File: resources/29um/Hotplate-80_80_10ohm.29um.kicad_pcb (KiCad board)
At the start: 2 copper layers, 80 x 80 mm, 7 parts, among them J1 Hotplate_Power_Connection, J2 Hotplate_Power_Connection

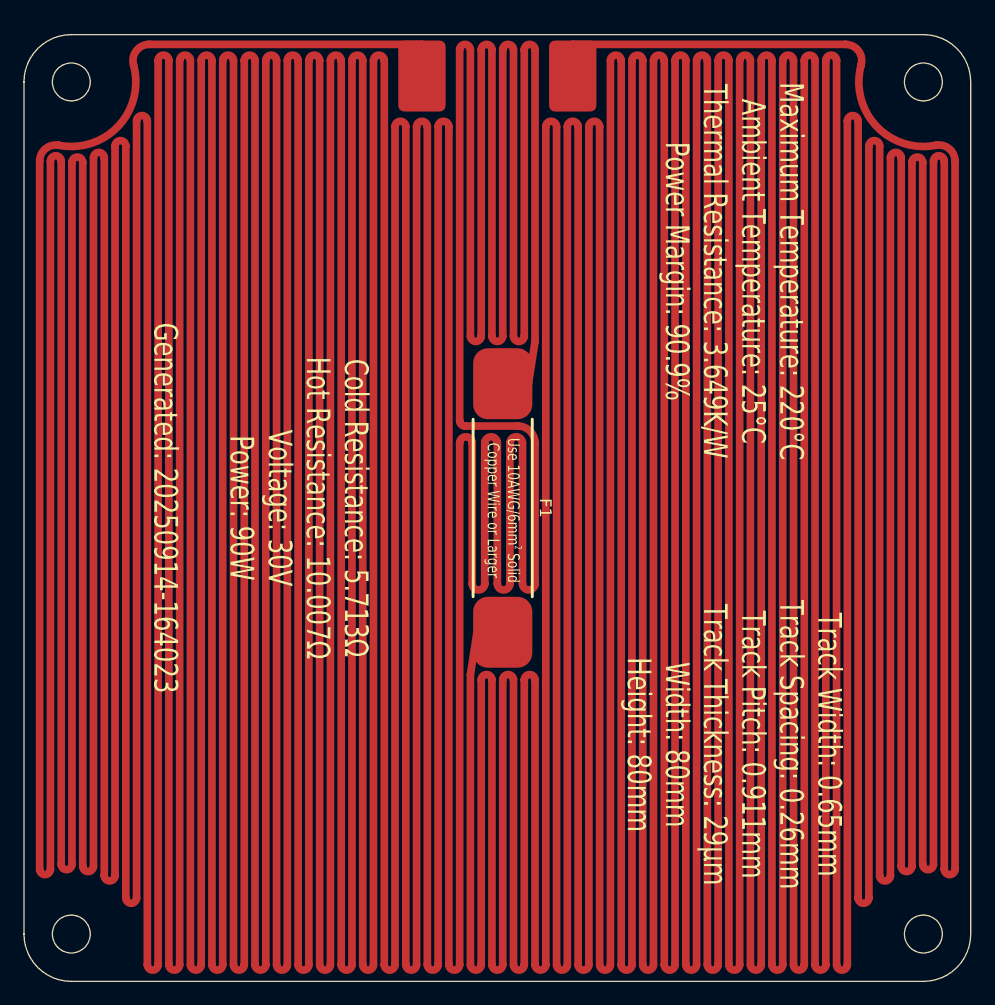
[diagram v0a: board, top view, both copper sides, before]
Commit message: Replaced obsolete 25mm thermal fuse footprint with new 35mm thermal fuse footprint.
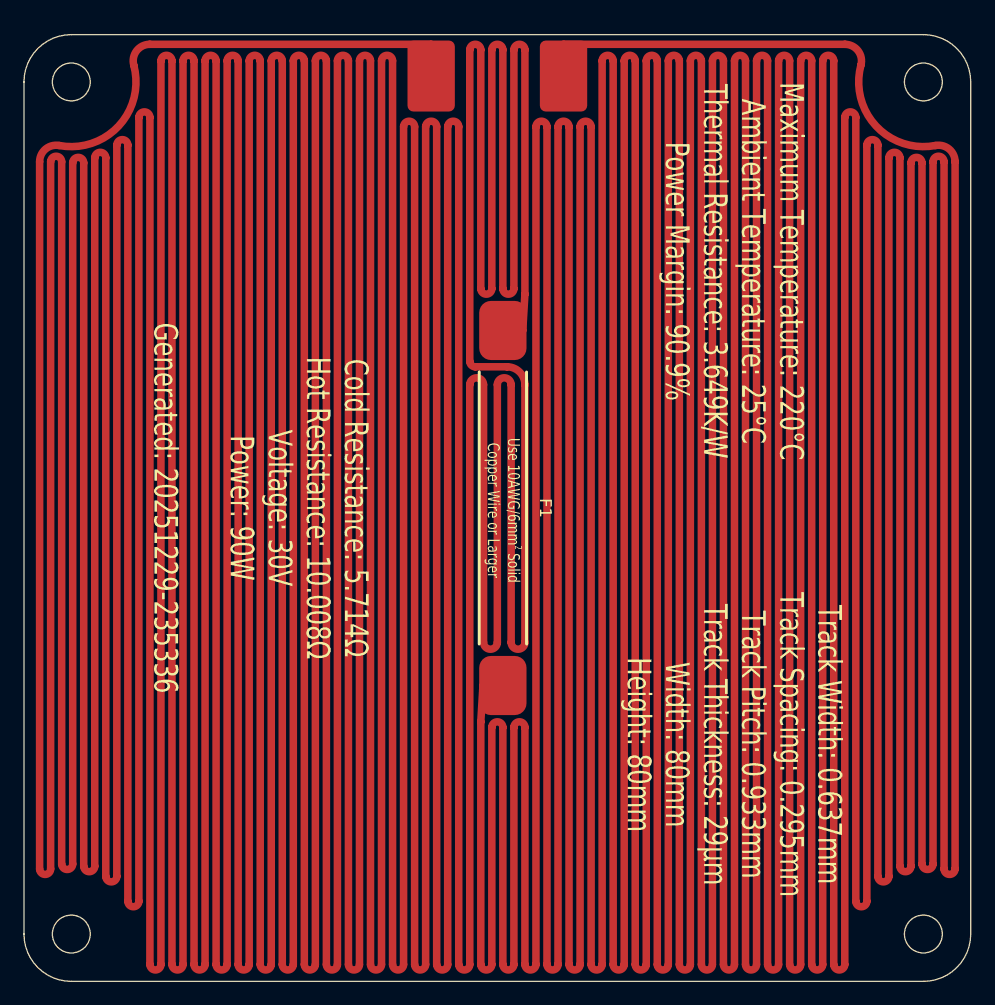
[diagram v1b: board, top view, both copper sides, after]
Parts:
- F1: footprint blg:Thermal Fuse, Front, 25mm -> blg:Thermal Fuse, SN100C, Front, 35mm
- moved J2 0.78 mm to (110.6, 68.5)
- moved J1 0.78 mm to (99.4, 68.5)
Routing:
- net Net-(J2-Pin_1): track 3059.8 -> 2989.9 mm
- net Net-(J1-Pin_1): track 3225.1 -> 3166.7 mm
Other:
- board text added: "Cold Resistance: 5.714Ω Hot Resistance: 10.008Ω Voltage: 30V Power: 90W Generated: 20251229-235336"
- board text added: "Track Width: 0.637mm Track Spacing: 0.295mm Track Pitch: 0.933mm Track Thickness: 29µm Width: 80mm Height: 80mm"
- board text removed: "Cold Resistance: 5.713Ω Hot Resistance: 10.007Ω Voltage: 30V Power: 90W Generated: 20250914-164023"
- board text removed: "Track Width: 0.65mm Track Spacing: 0.26mm Track Pitch: 0.911mm Track Thickness: 29µm Width: 80mm Height: 80mm"
